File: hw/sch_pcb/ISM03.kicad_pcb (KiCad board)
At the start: 2 copper layers, 50.3 x 40.1 mm, 75 parts, among them J1 JUMP_3X2, J13 HEADER_2x01_PARALLEL, J14 HEADER_2x01_PARALLEL, J15 HEADER_2x01_PARALLEL, J16 HEADER_2x01_PARALLEL, J17 HEADER_2x01_PARALLEL, J19 HEADER_2x01_PARALLEL, J2 MCX, J20 HEADER_2x01_PARALLEL, J21 HEADER_2x01_PARALLEL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

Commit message: Routing WiP.
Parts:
- removed J24, J25: HEADER_1x02, Mlab_Pin_Headers:Straight_1x02
- removed J26: HEADER_2x01_PARALLEL, Mlab_Pin_Headers:Straight_2x01
- added J6: HEADER_2x01_PARALLEL, Mlab_Pin_Headers:Straight_2x01, F.Cu at (134.5, 89.6)
- added J7: HEADER_2x01_PARALLEL, Mlab_Pin_Headers:Straight_2x01, F.Cu at (142.2, 89.6)
- U1: value LM1117-3V3 -> LM1117MP-3.3; footprint Mlab_IO:SOT-223 -> Package_TO_SOT_SMD:SOT-223-3_TabPin2
- moved J4 42.5 mm to (158.7, 118.6)
- moved C2 38.7 mm to (153.9, 123.5)
- moved J1 30.1 mm to (139.9, 118.0)
- moved C1 28.4 mm to (144.0, 121.0), turned to -90 degrees
- moved D1 26.0 mm to (135.0, 120.0), turned to -90 degrees
- moved C3 15.6 mm to (144.0, 115.6), turned to 90 degrees
- moved J17 15.3 mm to (128.2, 113.9), turned to 180 degrees
- moved C5 15.0 mm to (147.9, 113.4), turned to 0 degrees
- moved J20 14.1 mm to (128.2, 111.3), turned to 180 degrees
- moved J21 13.8 mm to (128.2, 108.8), turned to 180 degrees
- moved C19 8.07 mm to (136.7, 109.4)
- moved R16 7.98 mm to (132.8, 111.3), turned to 0 degrees
- moved L11 7.90 mm to (145.8, 111.1), turned to 0 degrees
- moved R17 7.45 mm to (132.8, 108.8), turned to 0 degrees
- moved R13 5.45 mm to (140.8, 109.4)
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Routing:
- net +3.3V: track 0.00 -> 25.4 mm
- net VCC: track 0.00 -> 22.6 mm
- net Net-(C15-Pad1): track 0.00 -> 10.9 mm
- net Net-(U2-~{SEL}): track 0.00 -> 9.73 mm
- net Net-(U2-GPIO0): track 0.00 -> 9.50 mm
- net Net-(U2-SDI): track 0.00 -> 7.86 mm
- net Net-(U2-GPIO1): track 0.00 -> 6.73 mm
- net Net-(U2-XOUT): track 0.00 -> 6.23 mm
- net /P0.1_1: track 0.00 -> 6.02 mm
- net Net-(U2-SCLK): track 0.00 -> 5.22 mm
- net Net-(U2-~{IRQ}): track 0.00 -> 5.05 mm
- net Net-(U2-XIN): track 0.00 -> 3.62 mm
- net Net-(U2-TXRAMP): track 0.00 -> 2.28 mm
- net GND: vias 79 -> 63
- net /SDO: vias 1 -> 0
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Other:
- board text added: "IN 5-10V"
- board text removed: "IN 5-12V"

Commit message: Roughtly routet PCB.
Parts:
- removed C10: 8,2pF, Capacitor_SMD:C_0805_2012Metric
- removed C8: 15pF, Capacitor_SMD:C_0805_2012Metric
- removed L2: 0R, Resistor_SMD:R_0805_2012Metric
- removed L4, L6: 18nH, Inductor_SMD:L_0805_2012Metric
- C11: value 8,2pF -> 9.1pF
- C12: value 2.7pF -> 2.2pF
- C13: value 5.1pF -> 4.7pF
- C4: value 6.8pf -> 10pF
- C6: value 6.8pf -> 100pF
- C7: value 15pF -> 12pF
- C9: value 8,2pF -> 15pF
- L1: value 0R -> 22nH
- L10: value 56nH -> 62nH
- L3: value 18nH -> 36nH
- L5: value 18nH -> 30nH
- L7: value 39nH -> 33nH
- moved C6 8.46 mm to (152.9, 100.1), turned to 0 degrees
- moved L1 7.70 mm to (165.1, 109.4)
- moved C13 7.01 mm to (146.2, 99.2)
- moved L8 6.25 mm to (144.2, 105.9)
- moved L3 5.86 mm to (160.4, 107.9), turned to 135 degrees
- moved L10 5.08 mm to (145.0, 102.0), turned to -45 degrees
- moved C4 5.07 mm to (161.7, 110.5), turned to -135 degrees
- moved L9 4.18 mm to (149.1, 100.1)
- moved C12 3.58 mm to (149.1, 102.0)
- moved L5 2.83 mm to (155.8, 104.9)
- moved L7 2.82 mm to (150.2, 104.9)
- moved R1 2.78 mm to (146.5, 108.4)
- moved R4 2.52 mm to (144.7, 94.0)
- moved C11 2.12 mm to (146.7, 104.9), turned to 0 degrees
- moved R5 2.05 mm to (147.6, 93.2)
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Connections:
- C12 pad 2: Net-(C10-Pad1) -> Net-(C12-Pad2)
- C6 pad 1: Net-(C6-Pad1) -> Net-(C12-Pad2)
- C6 pad 2: GND -> Net-(C6-Pad2)
- J3 pad 1: Net-(J3-Pad1) -> Net-(C6-Pad2)
- L9 pad 1: Net-(C10-Pad1) -> Net-(C12-Pad2)
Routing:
- net +3.3V: track 25.4 -> 91.5 mm, vias 0 -> 2
- net Net-(J6-Pad1): track 0.00 -> 16.5 mm
- net /TXRAMP: track 0.00 -> 15.6 mm
- net Net-(C6-Pad2): track 0.00 -> 15.6 mm
- net Net-(U2-GPIO2): track 0.00 -> 12.4 mm
- net Net-(U2-GPIO3): track 0.00 -> 10.7 mm
- net Net-(J7-Pad1): track 0.00 -> 10.3 mm
- net Net-(U2-SDN): track 0.00 -> 9.40 mm
- net Net-(J2-Pad1): track 10.7 -> 2.81 mm
- net Net-(C15-Pad1): track 10.9 -> 18.0 mm
- net /SDN: track 0.00 -> 6.81 mm, vias 0 -> 2
- net Net-(C10-Pad1): track 6.61 -> 0.00 mm
- net Net-(J3-Pad1): track 6.03 -> 0.00 mm
- net /nIRQ: track 0.00 -> 4.93 mm
- net /GPIO1: track 0.00 -> 4.93 mm
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
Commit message: Fix silksceen.
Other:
- board text added: "#SEL"
- board text added: "GPIO0"
- board text added: "GPIO1"
- board text added: "GPIO2"
- board text added: "GPIO3"
- board text added: "LEDG"
- board text added: "LEDR"
- board text added: "SCLK"
- board text added: "SDI"
- board text added: "SDN"
- board text added: "SDO"
- board text removed: "GND"
- board text removed: "GP0"
- board text removed: "GP1"
- board text removed: "GP2"
- board text removed: "GP3"
- board text removed: "LED"
- board text removed: "P0.6"
- board text removed: "P1.4"
- board text removed: "P1.5"
- board text removed: "P1.6"
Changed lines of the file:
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@@
 		)
 		(property "UST_ID" "5c70984812875079b91f8ba2"
-			(at 242.505236 -56.506858 360)
+			(at 242.505236 -56.506858 0)
 			(layer "B.Fab")
 			(hide yes)
@@
 		(tags "capacitor")
 		(property "Reference" "C11"
-			(at 0 1.679999 360)
+			(at 0 1.679999 0)
 			(layer "B.SilkS")
 			(effects
@@
 		)
 		(property "Value" "9.1pF"
-			(at 0 -1.679999 360)
+			(at 0 -1.679999 0)
 			(layer "B.Fab")
 			(effects
@@
 		)
 		(property "Footprint" "Capacitor_SMD:C_0805_2012Metric"
-			(at 0 0 360)
+			(at 0 0 0)
 			(layer "F.Fab")
 			(hide yes)
@@
 		)
 		(property "Datasheet" ""
-			(at 0 0 360)
+			(at 0 0 0)
 			(layer "F.Fab")
 			(hide yes)
@@
 		)
 		(property "Description" ""
-			(at 0 0 360)
+			(at 0 0 0)
 			(layer "F.Fab")
 			(hide yes)
@@
 		)
 		(fp_text user "${REFERENCE}"
-			(at 0 0 360)
+			(at 0 0 0)
 			(layer "B.Fab")
 			(effects
@@
 		(tags "capacitor")
 		(property "Reference" "C6"
-			(at 0 1.679999 360)
+			(at 0 1.679999 0)
 			(layer "B.SilkS")
 			(effects
@@
 		)
 		(property "Value" "100pF"
-			(at 0 -1.679999 360)
+			(at 0 -1.679999 0)
 			(layer "B.Fab")
 			(effects
@@
 		)
 		(property "Footprint" "Capacitor_SMD:C_0805_2012Metric"
-			(at 0 0 360)
+			(at 0 0 0)
 			(layer "F.Fab")
 			(hide yes)
@@
 		)
 		(property "Datasheet" ""
-			(at 0 0 360)
+			(at 0 0 0)
 			(layer "F.Fab")
 			(hide yes)
@@
 		)
 		(property "Description" ""
-			(at 0 0 360)
+			(at 0 0 0)
 			(layer "F.Fab")
 			(hide yes)
@@
 		)
 		(fp_text user "${REFERENCE}"
-			(at 0 0 360)
+			(at 0 0 0)
 			(layer "B.Fab")
 			(effects
@@
 		(layer "Edge.Cuts")
 	)
-	(gr_text "P1.6"
-		(at 134.520047 91.030689 90)
+	(gr_text "LEDR"
+		(at 134.657 92.173 90)
 		(layer "F.SilkS")
 		(effects
@@
 		)
 	)
-	(gr_text "P1.5"
-		(at 137.060047 91.030689 90)
+	(gr_text "LEDG"
+		(at 142.277 92.173 90)
 		(layer "F.SilkS")
 		(effects
@@
 		)
 	)
-	(gr_text "P1.4"
-		(at 139.600047 91.030689 90)
+	(gr_text "SDN"
+		(at 144.817 92.172311 90)
 		(layer "F.SilkS")
 		(effects
@@
 		)
 	)
-	(gr_text "GP2"
-		(at 142.140047 91.030689 90)
+	(gr_text "GPIO2"
+		(at 137.197 92.173 90)
 		(layer "F.SilkS")
 		(effects
@@
 		)
 	)
-	(gr_text "GP3"
-		(at 144.680047 91.030689 90)
+	(gr_text "GPIO3"
+		(at 139.737 92.173 90)
 		(layer "F.SilkS")
 		(effects
@@
 		)
 	)
-	(gr_text "GND"
-		(at 135.155047 120.240689 90)
+	(gr_text "SDO"
+		(at 135.2666 101.4186 0)
 		(layer "F.SilkS")
 		(effects
@@
 		)
 	)
-	(gr_text "P0.6"
-		(at 137.695047 120.240689 90)
+	(gr_text "SCLK"
+		(at 136.1556 103.8062 0)
 		(layer "F.SilkS")
 		(effects
@@
 	)
 	(gr_text "#IRQ"
-		(at 140.235047 120.240689 90)
+		(at 135.9778 106.3716 0)
 		(layer "F.SilkS")
 		(effects
@@
 		)
 	)
-	(gr_text "GP1"
-		(at 142.775047 120.240689 90)
+	(gr_text "GPIO1"
+		(at 136.943 111.4262 0)
 		(layer "F.SilkS")
 		(effects
@@
 	)
 	(gr_text "RAMP"
-		(at 147.855047 109.445689 90)
+		(at 136.2572 114.1694 0)
 		(layer "F.SilkS")
 		(effects
@@
 		)
 	)
-	(gr_text "GP0"
-		(at 145.315047 120.240689 90)
+	(gr_text "GPIO0"
+		(at 136.943 108.8354 0)
 		(layer "F.SilkS")
 		(effects
@@
 		)
 	)
-	(gr_text "P1.4"
-		(at 154.205047 112.620689 90)
+	(gr_text "IN 5-10V"
+		(at 143.8772 118.335 90)
 		(layer "F.SilkS")
 		(effects
@@
 				(thickness 0.3)
 			)
-			(justify right)
-		)
-	)
-	(gr_text "P1.5"
-		(at 151.665047 112.620689 90)
-		(layer "F.SilkS")
-		(effects
-			(font
-				(size 1.3 1.3)
-				(thickness 0.3)
-			)
-			(justify right)
-		)
-	)
-	(gr_text "LED"
-		(at 152.808047 123.796689 0)
-		(layer "F.SilkS")
-		(effects
-			(font
-				(size 1.3 1.3)
-				(thickness 0.3)
-			)
-		)
-	)
-	(gr_text "IN 5-10V"
-		(at 121.312047 98.650689 90)
-		(layer "F.SilkS")
-		(effects
-			(font
-				(size 1.3 1.3)
-				(thickness 0.3)
-			)
 		)
 	)
 	(gr_text "OUT 3V3"
-		(at 121.058047 111.604689 90)
+		(at 162.724 118.6144 90)
 		(layer "F.SilkS")
 		(effects
@@
 	)
 	(gr_text "2024"
-		(at 159.920047 90.522689 0)
+		(at 154.6976 111.7056 0)
 		(layer "F.SilkS")
 		(effects
@@
 	)
 	(gr_text "kaklik"
-		(at 159.920047 87.728689 0)
+		(at 154.6468 109.4704 0)
 		(layer "F.SilkS")
 		(effects
@@
 		)
 	)
+	(gr_text "LEDG"
+		(at 159.4982 91.3348 0)
+		(layer "F.SilkS")
+		(effects
+			(font
+				(size 1.3 1.3)
+				(thickness 0.3)
+			)
+			(justify right)
+		)
+	)
+	(gr_text "LEDR"
+		(at 159.5744 87.1692 0)
+		(layer "F.SilkS")
+		(effects
+			(font
+				(size 1.3 1.3)
+				(thickness 0.3)
+			)
+			(justify right)
+		)
+	)
+	(gr_text "SDI"
+		(at 135.1904 98.7516 0)
+		(layer "F.SilkS")
+		(effects
+			(font
+				(size 1.3 1.3)
+				(thickness 0.3)
+			)
+			(justify right)
+		)
+	)
+	(gr_text "#SEL"
+		(at 132.244 92.4524 90)
+		(layer "F.SilkS")
+		(effects
+			(font
+				(size 1.3 1.3)
+				(thickness 0.3)
+			)
+			(justify right)
+		)
+	)

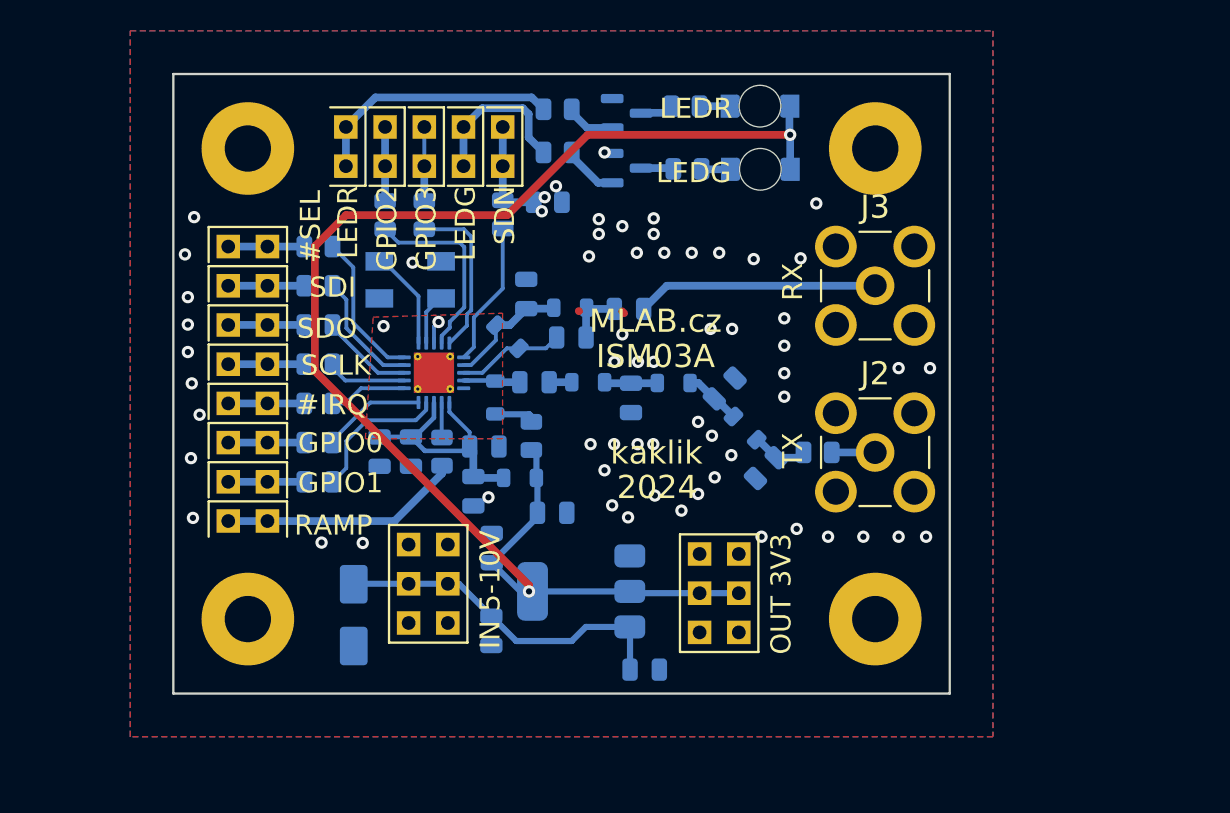
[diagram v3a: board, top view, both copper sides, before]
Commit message: Cleanup layout. Correcly move References and texts.
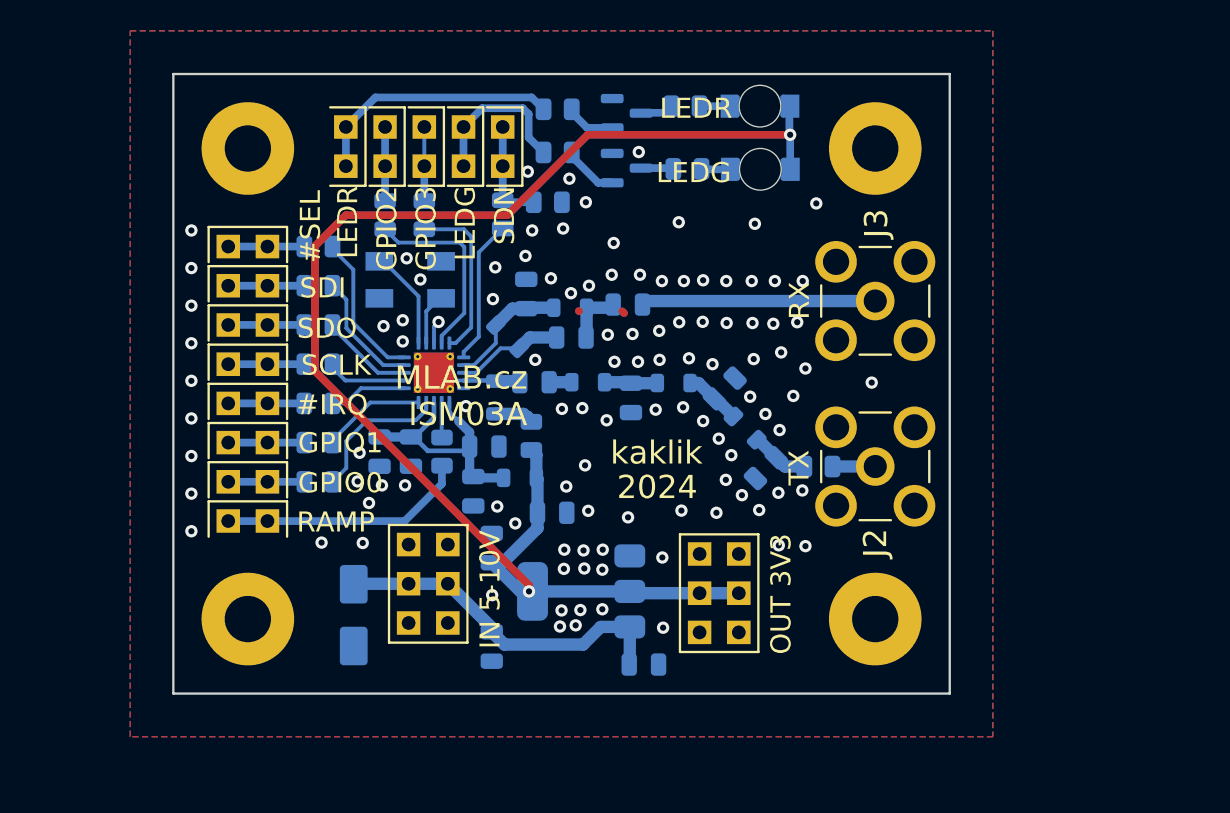
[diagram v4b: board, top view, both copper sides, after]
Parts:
- moved C1 1.02 mm to (144.0, 122.0)
- moved J3 0.99 mm to (168.8, 99.6)
- moved L1 0.92 mm to (165.1, 110.4)
- moved J2 0.91 mm to (168.8, 110.4)
- moved C2 0.33 mm to (153.8, 123.2)
- moved C6 0.29 mm to (152.8, 99.9)
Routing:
- net +3.3V: track 91.5 -> 98.3 mm
- net VCC: track 22.6 -> 28.6 mm
- net Net-(C12-Pad2): track 3.77 -> 7.27 mm
- net Net-(L8-Pad1): track 2.42 -> 4.97 mm
- net Net-(U2-RXp): track 7.95 -> 9.70 mm
- net Net-(C9-Pad1): track 3.45 -> 4.97 mm
- net Net-(U2-TX): track 3.68 -> 5.05 mm
- net /SDN: track 6.81 -> 6.64 mm, vias 2 -> 0
- net GND: vias 62 -> 108

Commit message: Improve Layout, silkscreen Update footprint from libraries.
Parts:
- moved C3 1.63 mm to (144.2, 117.3)
- moved C5 0.24 mm to (147.8, 113.6)
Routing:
- net +3.3V: track 98.3 -> 101.1 mm
